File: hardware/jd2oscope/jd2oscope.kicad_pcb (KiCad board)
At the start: 2 copper layers, 57 parts, among them J1 9V_CONN, J2 CONBNC001, J3 CONBNC001, U1 ESP32-DEVKITC-32D, U2 ILI9341-320x240-TFT-Touch, U3 NCP1117-5.0_SOT223, U4 OPA192IDBVR, U5 ADS7279IPW, U6 OPA192IDBVR, U7 ADS7279IPW

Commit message: feat: pcb progress
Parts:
- added REF**: MountingHole_4.3mm_M4_DIN965_Pad, MountingHole:MountingHole_4.3mm_M4_DIN965_Pad, F.Cu at (106.2, 144.2)
- added REF**: MountingHole_4.3mm_M4_DIN965_Pad, MountingHole:MountingHole_4.3mm_M4_DIN965_Pad, F.Cu at (168.2, 144.2)
- added REF**: MountingHole_4.3mm_M4_DIN965_Pad, MountingHole:MountingHole_4.3mm_M4_DIN965_Pad, F.Cu at (168.2, 32.2)
- added REF**: MountingHole_4.3mm_M4_DIN965_Pad, MountingHole:MountingHole_4.3mm_M4_DIN965_Pad, F.Cu at (106.2, 32.2)
- moved S1 90.8 mm to (121.2, 133.8)
- moved J1 87.0 mm to (108.5, 131.2), turned to -90 degrees
- moved C4 81.3 mm to (138.8, 139.0), turned to 90 degrees
- moved D1 80.3 mm to (128.9, 133.8), turned to 180 degrees
- moved C5 79.1 mm to (137.3, 139.0), turned to -90 degrees
- moved U3 71.7 mm to (141.2, 133.7)
- moved D2 69.6 mm to (133.5, 127.6), turned to 90 degrees
- moved C7 69.1 mm to (147.2, 135.5)
- moved C6 67.8 mm to (147.2, 131.8)
- moved R2 65.7 mm to (133.5, 131.4), turned to 90 degrees
- moved VR6 59.1 mm to (159.6, 105.8)
- moved VR5 51.7 mm to (159.6, 90.5)
- moved S3 50.9 mm to (160.3, 78.3)
- moved R1 46.5 mm to (110.1, 84.8)
- moved VR4 40.6 mm to (150.2, 78.5)
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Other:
- board outline added: 70 x 120 mm

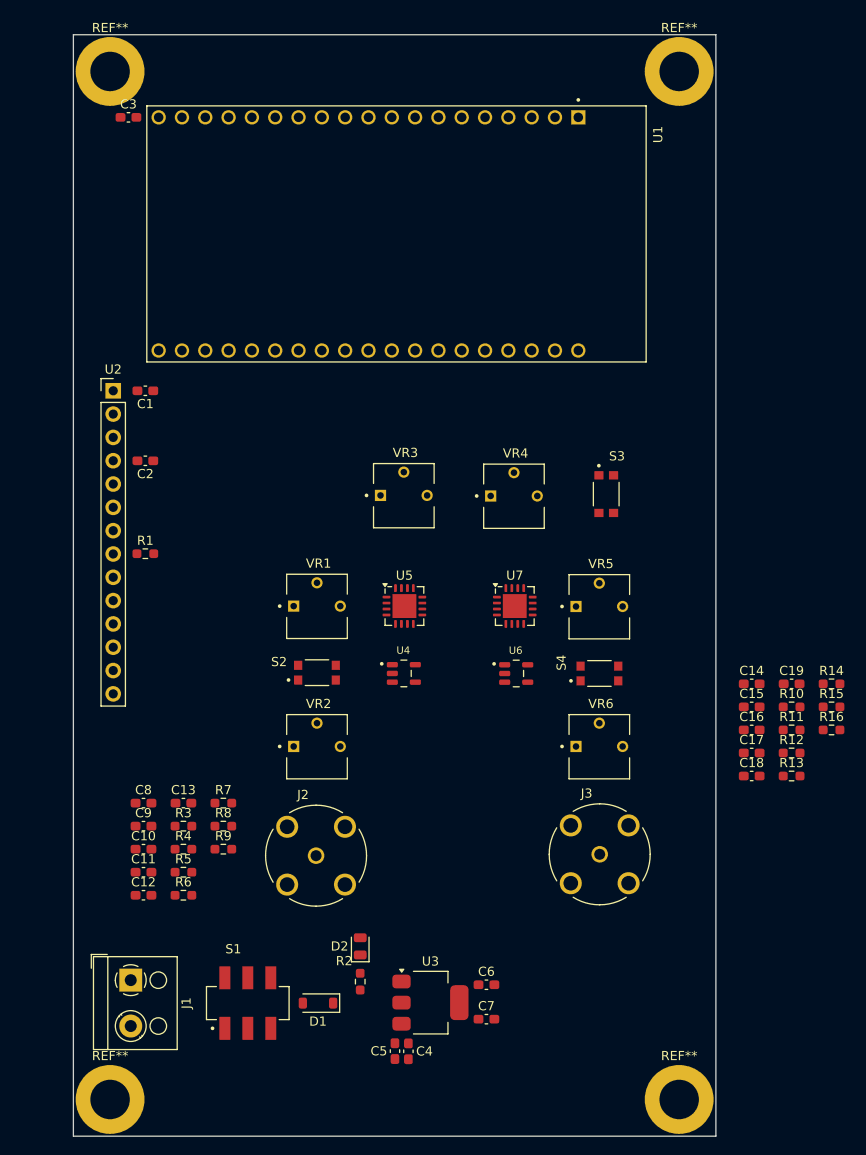
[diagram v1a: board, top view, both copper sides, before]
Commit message: feat: pcb complete
ha gottem
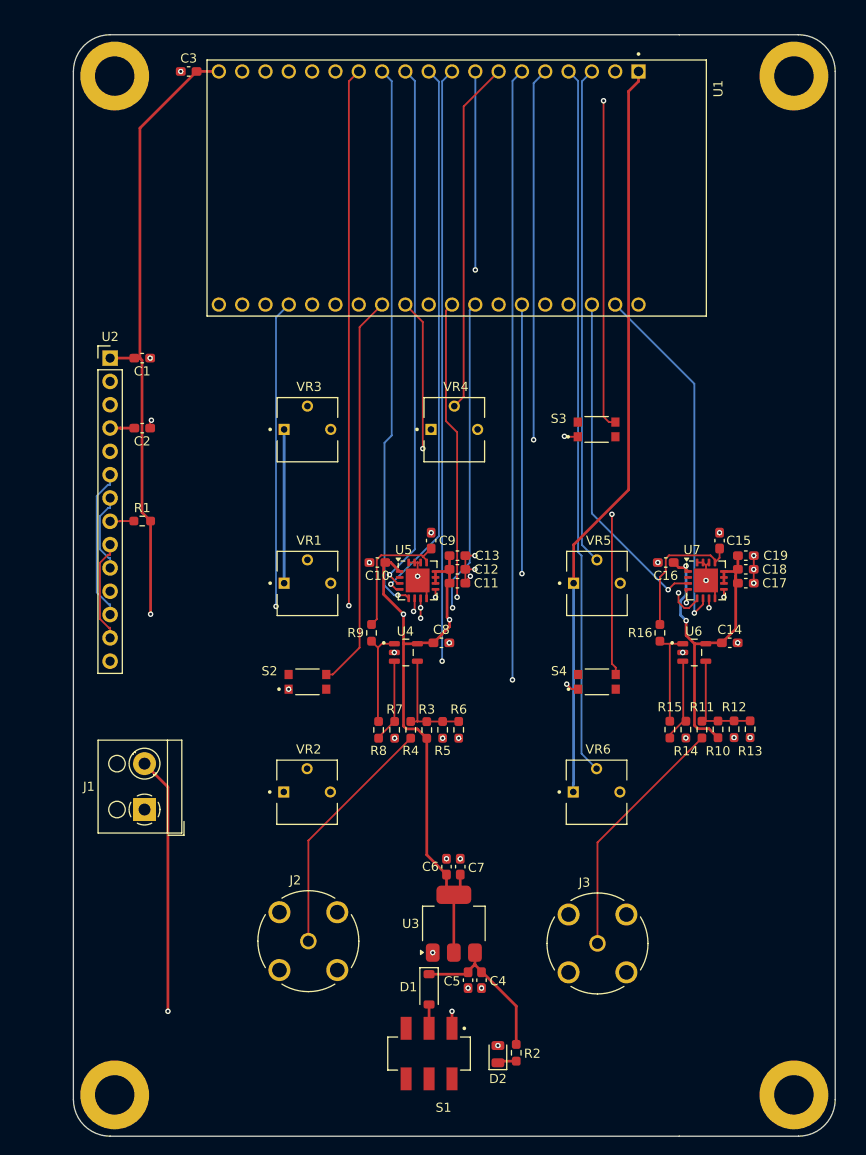
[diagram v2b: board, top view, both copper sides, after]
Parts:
- moved C12 49.3 mm to (144.1, 86.5)
- moved C11 46.5 mm to (144.1, 88.0)
- moved C9 44.2 mm to (141.2, 83.4), turned to 90 degrees
- moved C10 40.3 mm to (135.4, 85.8), turned to 180 degrees
- moved C13 40.2 mm to (144.1, 85.0)
- moved C8 36.9 mm to (142.3, 94.5)
- moved R6 35.0 mm to (144.2, 104.0), turned to -90 degrees
- moved R5 32.2 mm to (142.5, 104.0), turned to -90 degrees
- moved R9 28.6 mm to (134.7, 93.4), turned to 90 degrees
- moved R3 28.5 mm to (140.8, 104.0), turned to -90 degrees
- moved R4 28.0 mm to (139.0, 104.0), turned to -90 degrees
- moved C18 22.5 mm to (175.5, 86.5)
- moved R16 21.5 mm to (166.2, 93.4), turned to 90 degrees
- moved U7 21.0 mm to (171.2, 87.7)
- moved C16 20.5 mm to (166.8, 85.8), turned to 180 degrees
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- renumbered REF** to REF1, REF** to REF2, REF** to REF3, REF** to REF4
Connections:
- D1 pad 1: /5V_Regulator/PwrSwitch_Schottky -> /5V_Regulator/Schottky_LEDres-caps-5Vreg.In
- D1 pad 2: /5V_Regulator/Schottky_LEDres-caps-5Vreg.In -> /5V_Regulator/PwrSwitch_Schottky
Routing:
- net /reg.5V: track 0.00 -> 229.0 mm, vias 0 -> 5
- net /reg.3.3V: track 0.00 -> 201.2 mm
- net /SDI: track 0.00 -> 121.6 mm, vias 0 -> 2
- net /SDO: track 0.00 -> 114.7 mm, vias 0 -> 4
- net /SCK: track 0.00 -> 111.7 mm, vias 0 -> 3
- net /GPIO:touch_IRQ: track 0.00 -> 100.9 mm, vias 0 -> 1
- net /GPIO:ADC2_EOC/INT: track 0.00 -> 97.1 mm, vias 0 -> 2
- net /GPIO:signal1_timeShiftWiper: track 0.00 -> 93.1 mm, vias 0 -> 1
- net /GPIO:signal2_timeShiftWiper: track 0.00 -> 77.2 mm
- net /GPIO:signal1_ampShiftWiper: track 0.00 -> 70.9 mm, vias 0 -> 1
- net /GPIO:triggerBttn: track 0.00 -> 69.0 mm, vias 0 -> 1
- net /5V_Regulator/9V_PwrSwitch: track 0.00 -> 60.8 mm, vias 0 -> 2
- net /GPIO:ADC1_CS: track 0.00 -> 60.0 mm, vias 0 -> 1
- net /GPIO:ADC1_EOC/INT: track 0.00 -> 59.7 mm, vias 0 -> 1
- net /GPIO:ADC1_CONVST: track 0.00 -> 57.9 mm, vias 0 -> 1
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- added copper zone on In1.Cu, net GND
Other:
- board size 70 x 120 mm -> 83 x 120 mm
- copper layers 2 -> 4
- board text added: "3362P-1-103LF"
